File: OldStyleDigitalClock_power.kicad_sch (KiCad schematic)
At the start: 24 parts, among them J1 USB_A_OUT, J2 USB_A_OUT, J3 USB_C_IN, U11 NE555D

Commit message: Corrected Zener diode specs
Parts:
- D2: value 1N4734A -> W7
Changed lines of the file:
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@@
 			)
 		)
-		(property "Value" "1N4734A"
+		(property "Value" "W7"
 			(at 79.756 94.234 90)
 			(effects
@@
 			)
 		)
-		(property "Description" "Zener diode"
+		(property "Description" "Zener diode 5.6V"
 			(at 78.74 91.44 0)
 			(effects

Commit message: Changed units for caps
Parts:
- C11, C12: value 0.1 µF -> 100 nF
- D2: value W7 -> Zener 5.6V (W7)
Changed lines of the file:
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@@
 			)
 		)
-		(property "Value" "0.1 µF"
+		(property "Value" "100 nF"
 			(at 146.05 125.73 0)
 			(effects
@@
 			)
 		)
-		(property "Value" "W7"
+		(property "Value" "Zener 5.6V (W7)"
 			(at 79.756 94.234 90)
 			(effects
@@
 			)
 		)
-		(property "Value" "0.1 µF"
+		(property "Value" "100 nF"
 			(at 133.35 91.44 0)
 			(effects

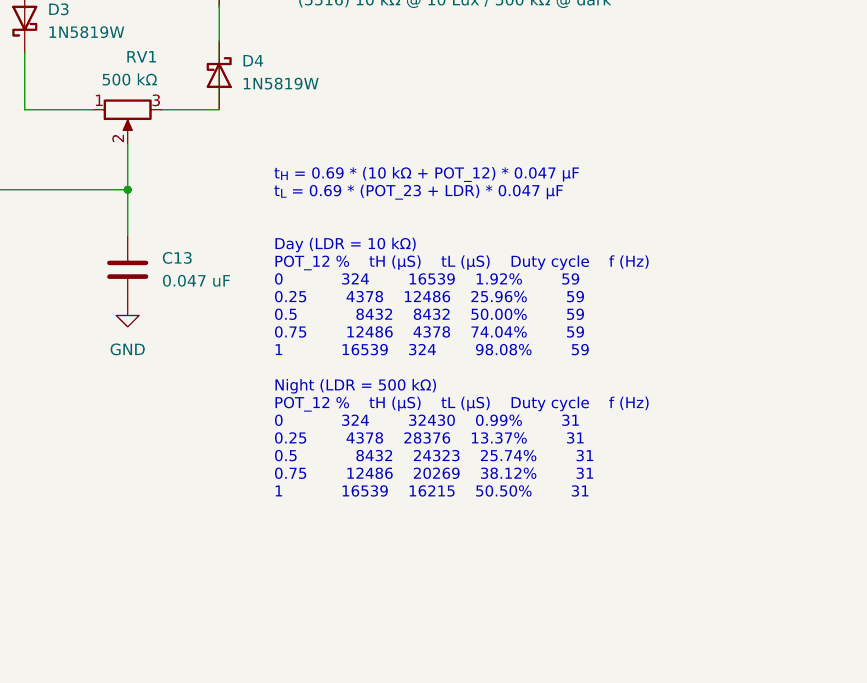
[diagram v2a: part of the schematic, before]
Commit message: Reduced C13 value to avoid visible flickering
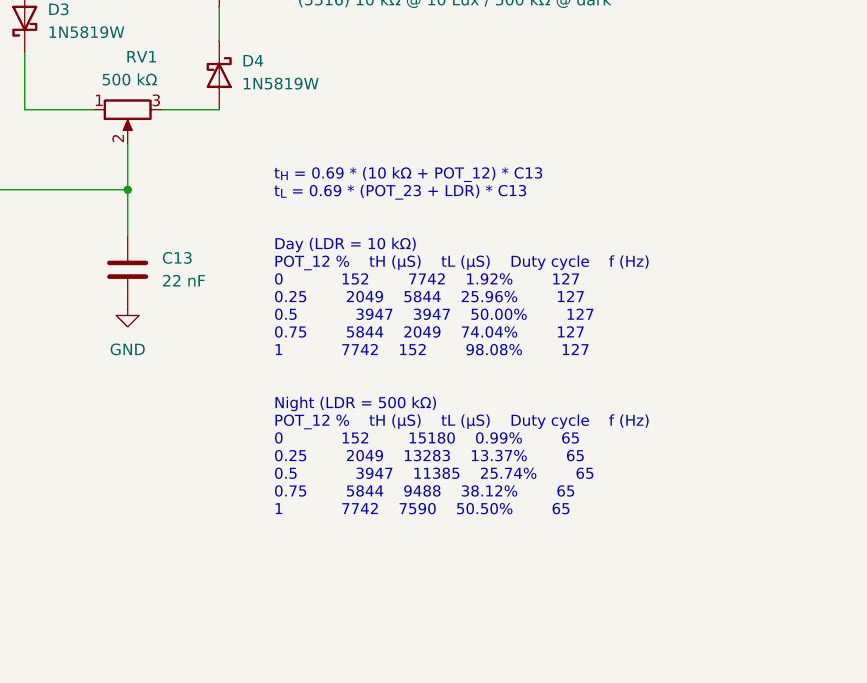
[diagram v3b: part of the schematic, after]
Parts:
- C13: value 0.047 uF -> 22 nF
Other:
- note added: "t_{H} = 0.69 * (10 kΩ + POT_12) * C13 t_{L} = 0.69 * (POT_23 + LDR) * C13 Day (LDR = 10 kΩ) POT_12 % tH (µS) tL (µS) Duty cycle f (Hz) 0 152 7742 1.92% 127 0.25 2049 5844 25.96% 127 0.5 3947 3947 50.00% 127 0.75 5844 2049 74.04% 127 1 7742 152 98.08% 127 Night (LDR = 500 kΩ) POT_12 % tH (µS) tL (µS) Duty cycle f (Hz) 0 152 15180 0.99% 65 0.25 2049 13283 13.37% 65 0.5 3947 11385 25.74% 65 0.75 584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"
- note removed: "t_{H} = 0.69 * (10 kΩ + POT_12) * 0.047 µF t_{L} = 0.69 * (POT_23 + LDR) * 0.047 µF Day (LDR = 10 kΩ) POT_12 % tH (µS) tL (µS) Duty cycle f (Hz) 0 324 16539 1.92% 59 0.25 4378 12486 25.96% 59 0.5 8432 8432 50.00% 59 0.75 12486 4378 74.04% 59 1 16539 324 98.08% 59 Night (LDR = 500 kΩ) POT_12 % tH (µS) tL (µS) Duty cycle f (Hz) 0 324 32430 0.99% 31 0.25 4378 28376 13.37% 31 0.5 8432 24323 25.74% 31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"
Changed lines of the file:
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@@
 		)
 	)
-	(text "t_{H} = 0.69 * (10 kΩ + POT_12) * 0.047 µF\nt_{L} = 0.69 * (POT_23 + LDR) * 0.047 µF\n\n\nDay (LDR = 10 kΩ)				\nPOT_12 %	tH (µS)	tL (µS)	Duty cycle	f (Hz)\n0			324		16539	1.92%		59\n0.25		4378	12486	25.96%		59\n0.5			8432	8432	50.00%		59\n0.75		12486	4378	74.04%		59\n1			16539	324		98.08%		59\n				\nNight (LDR = 500 kΩ)				\nPOT_12 %	tH (µS)	tL (µS)	Duty cycle	f (Hz)\n0			324		32430	0.99%		31\n0.25		4378	28376	13.37%		31\n0.5			8432	24323	25.74%		31\n0.75		12486	20269	38.12%		31\n1			16539	16215	50.50%		31\n"
+	(text "t_{H} = 0.69 * (10 kΩ + POT_12) * C13\nt_{L} = 0.69 * (POT_23 + LDR) * C13\n\n\nDay (LDR = 10 kΩ)				\nPOT_12 %	tH (µS)	tL (µS)	Duty cycle	f (Hz)\n0			152		7742	1.92%		127\n0.25		2049	5844	25.96%		127\n0.5			3947	3947	50.00%		127\n0.75		5844	2049	74.04%		127\n1			7742	152		98.08%		127\n\n				\nNight (LDR = 500 kΩ)				\nPOT_12 %	tH (µS)	tL (µS)	Duty cycle	f (Hz)\n0			152		15180	0.99%		65\n0.25		2049	13283	13.37%		65\n0.5			3947	11385	25.74%		65\n0.75		5844	9488	38.12%		65\n1			7742	7590	50.50%		65\n\n"
 		(exclude_from_sim no)
 		(at 229.616 112.014 0)
@@
 			)
 		)
-		(property "Value" "0.047 uF"
+		(property "Value" "22 nF"
 			(at 217.17 124.4599 0)
 			(effects

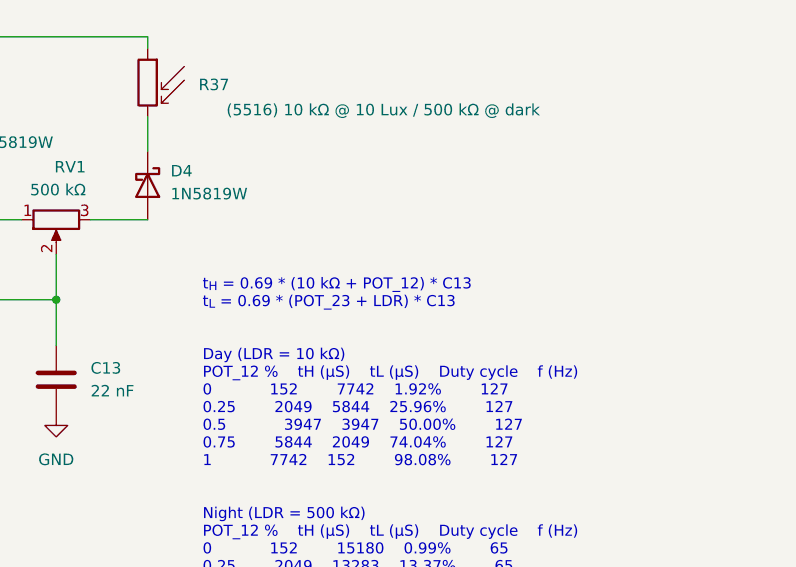
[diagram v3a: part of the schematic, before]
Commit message: Added missing reset connection for low digit of the hours
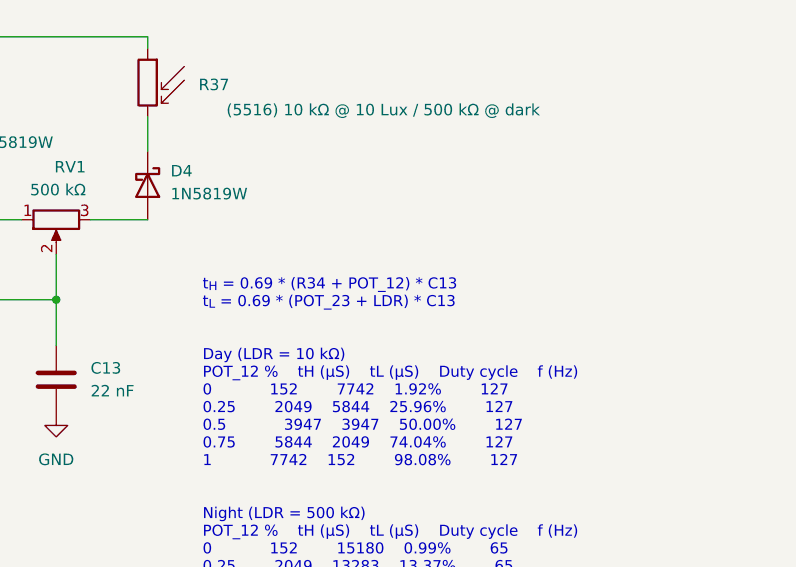
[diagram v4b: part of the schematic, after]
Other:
- note added: "t_{H} = 0.69 * (R34 + POT_12) * C13 t_{L} = 0.69 * (POT_23 + LDR) * C13 Day (LDR = 10 kΩ) POT_12 % tH (µS) tL (µS) Duty cycle f (Hz) 0 152 7742 1.92% 127 0.25 2049 5844 25.96% 127 0.5 3947 3947 50.00% 127 0.75 5844 2049 74.04% 127 1 7742 152 98.08% 127 Night (LDR = 500 kΩ) POT_12 % tH (µS) tL (µS) Duty cycle f (Hz) 0 152 15180 0.99% 65 0.25 2049 13283 13.37% 65 0.5 3947 11385 25.74% 65 0.75 5844 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"
- note removed: "t_{H} = 0.69 * (10 kΩ + POT_12) * C13 t_{L} = 0.69 * (POT_23 + LDR) * C13 Day (LDR = 10 kΩ) POT_12 % tH (µS) tL (µS) Duty cycle f (Hz) 0 152 7742 1.92% 127 0.25 2049 5844 25.96% 127 0.5 3947 3947 50.00% 127 0.75 5844 2049 74.04% 127 1 7742 152 98.08% 127 Night (LDR = 500 kΩ) POT_12 % tH (µS) tL (µS) Duty cycle f (Hz) 0 152 15180 0.99% 65 0.25 2049 13283 13.37% 65 0.5 3947 11385 25.74% 65 0.75 584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"
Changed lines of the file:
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@@
 		)
 	)
-	(text "t_{H} = 0.69 * (10 kΩ + POT_12) * C13\nt_{L} = 0.69 * (POT_23 + LDR) * C13\n\n\nDay (LDR = 10 kΩ)				\nPOT_12 %	tH (µS)	tL (µS)	Duty cycle	f (Hz)\n0			152		7742	1.92%		127\n0.25		2049	5844	25.96%		127\n0.5			3947	3947	50.00%		127\n0.75		5844	2049	74.04%		127\n1			7742	152		98.08%		127\n\n				\nNight (LDR = 500 kΩ)				\nPOT_12 %	tH (µS)	tL (µS)	Duty cycle	f (Hz)\n0			152		15180	0.99%		65\n0.25		2049	13283	13.37%		65\n0.5			3947	11385	25.74%		65\n0.75		5844	9488	38.12%		65\n1			7742	7590	50.50%		65\n\n"
+	(text "t_{H} = 0.69 * (R34 + POT_12) * C13\nt_{L} = 0.69 * (POT_23 + LDR) * C13\n\n\nDay (LDR = 10 kΩ)				\nPOT_12 %	tH (µS)	tL (µS)	Duty cycle	f (Hz)\n0			152		7742	1.92%		127\n0.25		2049	5844	25.96%		127\n0.5			3947	3947	50.00%		127\n0.75		5844	2049	74.04%		127\n1			7742	152		98.08%		127\n\n				\nNight (LDR = 500 kΩ)				\nPOT_12 %	tH (µS)	tL (µS)	Duty cycle	f (Hz)\n0			152		15180	0.99%		65\n0.25		2049	13283	13.37%		65\n0.5			3947	11385	25.74%		65\n0.75		5844	9488	38.12%		65\n1			7742	7590	50.50%		65\n\n"
 		(exclude_from_sim no)
 		(at 229.616 112.014 0)

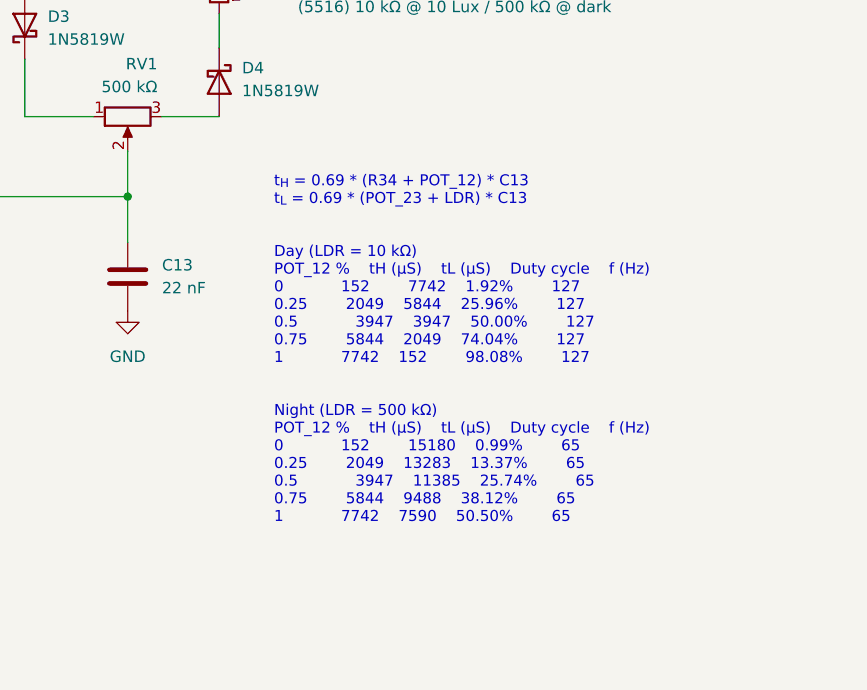
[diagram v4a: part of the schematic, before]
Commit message: Reduced C13 to 4.7 nF to account for stray capacitance and avoid flickering
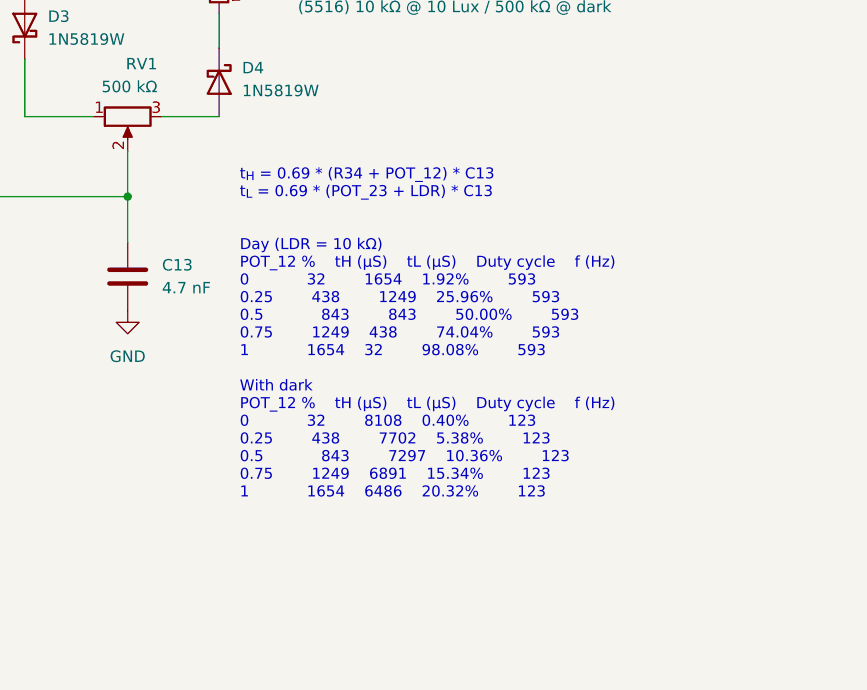
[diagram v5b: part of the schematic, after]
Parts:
- C13: value 22 nF -> 4.7 nF
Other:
- note added: "t_{H} = 0.69 * (R34 + POT_12) * C13 t_{L} = 0.69 * (POT_23 + LDR) * C13 Day (LDR = 10 kΩ) POT_12 % tH (µS) tL (µS) Duty cycle f (Hz) 0 32 1654 1.92% 593 0.25 438 1249 25.96% 593 0.5 843 843 50.00% 593 0.75 1249 438 74.04% 593 1 1654 32 98.08% 593 With dark POT_12 % tH (µS) tL (µS) Duty cycle f (Hz) 0 32 8108 0.40% 123 0.25 438 7702 5.38% 123 0.5 843 7297 10.36% 123 0.75 1249 6891 15.34% 123 1 165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"
- note removed: "t_{H} = 0.69 * (R34 + POT_12) * C13 t_{L} = 0.69 * (POT_23 + LDR) * C13 Day (LDR = 10 kΩ) POT_12 % tH (µS) tL (µS) Duty cycle f (Hz) 0 152 7742 1.92% 127 0.25 2049 5844 25.96% 127 0.5 3947 3947 50.00% 127 0.75 5844 2049 74.04% 127 1 7742 152 98.08% 127 Night (LDR = 500 kΩ) POT_12 % tH (µS) tL (µS) Duty cycle f (Hz) 0 152 15180 0.99% 65 0.25 2049 13283 13.37% 65 0.5 3947 11385 25.74% 65 0.75 5844 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"
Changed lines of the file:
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@@
 		)
 	)
-	(text "t_{H} = 0.69 * (R34 + POT_12) * C13\nt_{L} = 0.69 * (POT_23 + LDR) * C13\n\n\nDay (LDR = 10 kΩ)				\nPOT_12 %	tH (µS)	tL (µS)	Duty cycle	f (Hz)\n0			152		7742	1.92%		127\n0.25		2049	5844	25.96%		127\n0.5			3947	3947	50.00%		127\n0.75		5844	2049	74.04%		127\n1			7742	152		98.08%		127\n\n				\nNight (LDR = 500 kΩ)				\nPOT_12 %	tH (µS)	tL (µS)	Duty cycle	f (Hz)\n0			152		15180	0.99%		65\n0.25		2049	13283	13.37%		65\n0.5			3947	11385	25.74%		65\n0.75		5844	9488	38.12%		65\n1			7742	7590	50.50%		65\n\n"
+	(text "t_{H} = 0.69 * (R34 + POT_12) * C13\nt_{L} = 0.69 * (POT_23 + LDR) * C13\n\n\nDay (LDR = 10 kΩ)				\nPOT_12 %	tH (µS)	tL (µS)	Duty cycle	f (Hz)\n0			32		1654	1.92%		593\n0.25		438		1249	25.96%		593\n0.5			843		843		50.00%		593\n0.75		1249	438		74.04%		593\n1			1654	32		98.08%		593\n				\nWith dark				\nPOT_12 %	tH (µS)	tL (µS)	Duty cycle	f (Hz)\n0			32		8108	0.40%		123\n0.25		438		7702	5.38%		123\n0.5			843		7297	10.36%		123\n0.75		1249	6891	15.34%		123\n1			1654	6486	20.32%		123\n\n\n\n"
 		(exclude_from_sim no)
-		(at 229.616 112.014 0)
+		(at 225.806 111.252 0)
 		(effects
 			(font
@@
 			)
 		)
-		(property "Value" "22 nF"
+		(property "Value" "4.7 nF"
 			(at 217.17 124.4599 0)
 			(effects

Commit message: Updated comment
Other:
- note added: "t_{H} = 0.69 * (R34 + POT_12) * C13 t_{L} = 0.69 * (POT_23 + LDR) * C13 Day (R37 = 10 kΩ) POT_12 % tH (µS) tL (µS) Duty cycle f (Hz) 0 32 1654 1.92% 593 0.25 438 1249 25.96% 593 0.5 843 843 50.00% 593 0.75 1249 438 74.04% 593 1 1654 32 98.08% 593 With dark (R37 = 500 kΩ) POT_12 % tH (µS) tL (µS) Duty cycle f (Hz) 0 32 8108 0.40% 123 0.25 438 7702 5.38% 123 0.5 843 7297 10.36% 123 0.75 1249 6891 1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"
- note removed: "t_{H} = 0.69 * (R34 + POT_12) * C13 t_{L} = 0.69 * (POT_23 + LDR) * C13 Day (LDR = 10 kΩ) POT_12 % tH (µS) tL (µS) Duty cycle f (Hz) 0 32 1654 1.92% 593 0.25 438 1249 25.96% 593 0.5 843 843 50.00% 593 0.75 1249 438 74.04% 593 1 1654 32 98.08% 593 With dark POT_12 % tH (µS) tL (µS) Duty cycle f (Hz) 0 32 8108 0.40% 123 0.25 438 7702 5.38% 123 0.5 843 7297 10.36% 123 0.75 1249 6891 15.34% 123 1 165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"
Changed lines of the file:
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@@
 		)
 	)
-	(text "t_{H} = 0.69 * (R34 + POT_12) * C13\nt_{L} = 0.69 * (POT_23 + LDR) * C13\n\n\nDay (LDR = 10 kΩ)				\nPOT_12 %	tH (µS)	tL (µS)	Duty cycle	f (Hz)\n0			32		1654	1.92%		593\n0.25		438		1249	25.96%		593\n0.5			843		843		50.00%		593\n0.75		1249	438		74.04%		593\n1			1654	32		98.08%		593\n				\nWith dark				\nPOT_12 %	tH (µS)	tL (µS)	Duty cycle	f (Hz)\n0			32		8108	0.40%		123\n0.25		438		7702	5.38%		123\n0.5			843		7297	10.36%		123\n0.75		1249	6891	15.34%		123\n1			1654	6486	20.32%		123\n\n\n\n"
+	(text "t_{H} = 0.69 * (R34 + POT_12) * C13\nt_{L} = 0.69 * (POT_23 + LDR) * C13\n\n\nDay (R37 = 10 kΩ)				\nPOT_12 %	tH (µS)	tL (µS)	Duty cycle	f (Hz)\n0			32		1654	1.92%		593\n0.25		438		1249	25.96%		593\n0.5			843		843		50.00%		593\n0.75		1249	438		74.04%		593\n1			1654	32		98.08%		593\n				\nWith dark (R37 = 500 kΩ)\nPOT_12 %	tH (µS)	tL (µS)	Duty cycle	f (Hz)\n0			32		8108	0.40%		123\n0.25		438		7702	5.38%		123\n0.5			843		7297	10.36%		123\n0.75		1249	6891	15.34%		123\n1			1654	6486	20.32%		123\n\n\n\n"
 		(exclude_from_sim no)
 		(at 225.806 111.252 0)

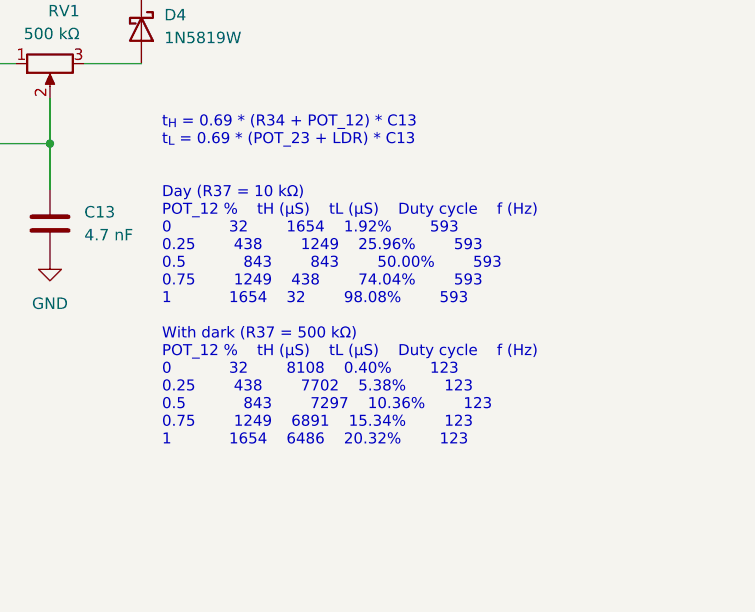
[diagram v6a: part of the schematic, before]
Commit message: Updated PWm schematics calculations
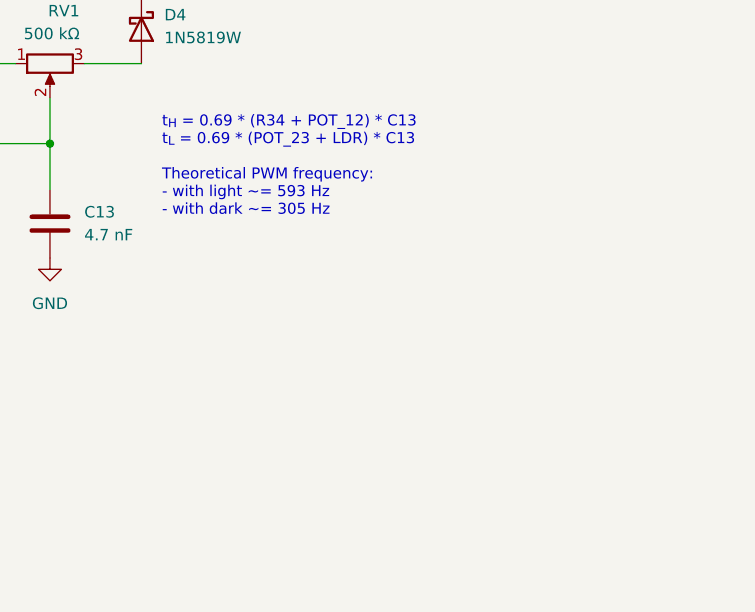
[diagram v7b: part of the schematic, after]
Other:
- note added: "t_{H} = 0.69 * (R34 + POT_12) * C13 t_{L} = 0.69 * (POT_23 + LDR) * C13 Theoretical PWM frequency: - with light ~= 593 Hz - with dark ~= 305 Hz"
- note removed: "t_{H} = 0.69 * (R34 + POT_12) * C13 t_{L} = 0.69 * (POT_23 + LDR) * C13 Day (R37 = 10 kΩ) POT_12 % tH (µS) tL (µS) Duty cycle f (Hz) 0 32 1654 1.92% 593 0.25 438 1249 25.96% 593 0.5 843 843 50.00% 593 0.75 1249 438 74.04% 593 1 1654 32 98.08% 593 With dark (R37 = 500 kΩ) POT_12 % tH (µS) tL (µS) Duty cycle f (Hz) 0 32 8108 0.40% 123 0.25 438 7702 5.38% 123 0.5 843 7297 10.36% 123 0.75 1249 6891 1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"
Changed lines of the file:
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@@
 		)
 	)
-	(text "t_{H} = 0.69 * (R34 + POT_12) * C13\nt_{L} = 0.69 * (POT_23 + LDR) * C13\n\n\nDay (R37 = 10 kΩ)				\nPOT_12 %	tH (µS)	tL (µS)	Duty cycle	f (Hz)\n0			32		1654	1.92%		593\n0.25		438		1249	25.96%		593\n0.5			843		843		50.00%		593\n0.75		1249	438		74.04%		593\n1			1654	32		98.08%		593\n				\nWith dark (R37 = 500 kΩ)\nPOT_12 %	tH (µS)	tL (µS)	Duty cycle	f (Hz)\n0			32		8108	0.40%		123\n0.25		438		7702	5.38%		123\n0.5			843		7297	10.36%		123\n0.75		1249	6891	15.34%		123\n1			1654	6486	20.32%		123\n\n\n\n"
+	(text "t_{H} = 0.69 * (R34 + POT_12) * C13\nt_{L} = 0.69 * (POT_23 + LDR) * C13\n\nTheoretical PWM frequency:\n- with light ~= 593 Hz\n- with dark ~= 305 Hz				\n\n\n\n\n"
 		(exclude_from_sim no)
 		(at 225.806 111.252 0)

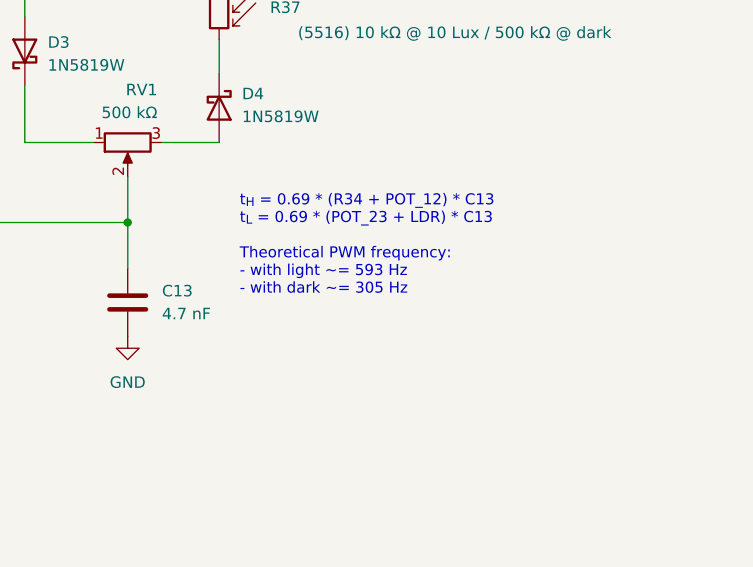
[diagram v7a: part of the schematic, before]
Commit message: Reduced C13 further while staying within the 555 limit of 100 kHz even when LDR may raise to several MΩ. This avoids flickering.
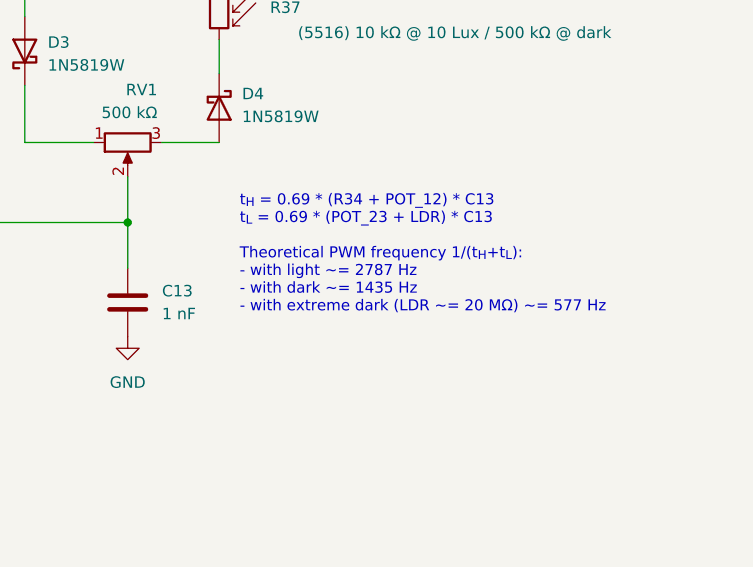
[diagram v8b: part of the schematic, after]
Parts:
- C13: value 4.7 nF -> 1 nF
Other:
- note added: "t_{H} = 0.69 * (R34 + POT_12) * C13 t_{L} = 0.69 * (POT_23 + LDR) * C13 Theoretical PWM frequency 1/(t_{H}+t_{L}): - with light ~= 2787 Hz - with dark ~= 1435 Hz - with extreme dark (LDR ~= 20 MΩ) ~= 577 Hz"
- note removed: "t_{H} = 0.69 * (R34 + POT_12) * C13 t_{L} = 0.69 * (POT_23 + LDR) * C13 Theoretical PWM frequency: - with light ~= 593 Hz - with dark ~= 305 Hz"
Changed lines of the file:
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@@
 		)
 	)
-	(text "t_{H} = 0.69 * (R34 + POT_12) * C13\nt_{L} = 0.69 * (POT_23 + LDR) * C13\n\nTheoretical PWM frequency:\n- with light ~= 593 Hz\n- with dark ~= 305 Hz				\n\n\n\n\n"
+	(text "t_{H} = 0.69 * (R34 + POT_12) * C13\nt_{L} = 0.69 * (POT_23 + LDR) * C13\n\nTheoretical PWM frequency 1/(t_{H}+t_{L}):\n- with light ~= 2787 Hz\n- with dark ~= 1435 Hz\n- with extreme dark (LDR ~= 20 MΩ) ~= 577 Hz\n\n\n\n"
 		(exclude_from_sim no)
 		(at 225.806 111.252 0)
@@
 			)
 		)
-		(property "Value" "4.7 nF"
+		(property "Value" "1 nF"
 			(at 217.17 124.4599 0)
 			(effects
